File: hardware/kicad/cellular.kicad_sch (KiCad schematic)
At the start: 46 parts, among them J4 SMN-304, J5 BWIPX-1-001E, Q1 S8050, Q2 S8050, Q5 S8050, Q6 S8050, U2 A7670C_24x24mm

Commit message: wip: revision 2
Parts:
- removed C31, C32: TBD, Capacitor_SMD:C_0402_1005Metric, symbol Device:C_Small
- removed D7: PESD0402, Capacitor_SMD:C_0402_1005Metric, symbol Device:D_TVS
- removed J5: BWIPX-1-001E, SAMTEC_RSP-122811-02:SAMTEC_RSP-122811-02, symbol RSP-122811-02:RSP-122811-02
- removed JP1: A7670_BOOT, Jumper:SolderJumper-2_P1.3mm_Open_RoundedPad1.0x1.5mm, symbol Jumper:SolderJumper_2_Open
- removed R13: 10k, Resistor_SMD:R_0402_1005Metric, symbol Device:R_Small
- removed R20, R21: 0, Resistor_SMD:R_0402_1005Metric, symbol Device:R_Small
- added C29: 33p, Capacitor_SMD:C_0402_1005Metric, symbol Device:C_Small
- added TP11: USB_BOOT, TestPoint:TestPoint_Pad_D1.0mm, symbol Connector:TestPoint
- added TP12: UART_LOG_TXD, TestPoint:TestPoint_Pad_D1.0mm, symbol Connector:TestPoint
- Q1, Q2: value S8050 -> PMBT3904
- TP1: value VBUS -> USB_DP; footprint TestPoint:TestPoint_Pad_D1.5mm -> TestPoint:TestPoint_Pad_D1.0mm; Distributor - -> (none); Distributor Link - -> (none); Distributor Part Number - -> (none); Id 47 -> (none); Manufacture - -> (none); Manufacture Part Number - -> (none); Type SMD -> (none)
- TP2: value USB_DP -> USB_DM; footprint TestPoint:TestPoint_Pad_D1.5mm -> TestPoint:TestPoint_Pad_D1.0mm; Distributor - -> (none); Distributor Link - -> (none); Distributor Part Number - -> (none); Id 48 -> (none); Manufacture - -> (none); Manufacture Part Number - -> (none); Type SMD -> (none)
- TP3: value USB_DM -> VBUS; footprint TestPoint:TestPoint_Pad_D1.5mm -> TestPoint:TestPoint_Pad_D1.0mm; Distributor - -> (none); Distributor Link - -> (none); Distributor Part Number - -> (none); Id 49 -> (none); Manufacture - -> (none); Manufacture Part Number - -> (none); Type SMD -> (none)
- TP4: value GND -> UART_LOG_RXD; footprint TestPoint:TestPoint_Pad_D1.5mm -> TestPoint:TestPoint_Pad_D1.0mm; Distributor - -> (none); Distributor Link - -> (none); Distributor Part Number - -> (none); Id 50 -> (none); Manufacture - -> (none); Manufacture Part Number - -> (none); Type SMD -> (none)
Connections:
- net GND: now also C29.2; no longer TP4.1
- net USIM_VDD: now also C29.1
- net CELL_ANT: now reaches U2.60 (RF_ANT)
- net UART_LOG_RXD: now reaches U2.22 (UART_LOG_RX)
- net UART_LOG_RXD: now also TP4.1
- net UART_LOG_TXD: now reaches U2.23 (UART_LOG_TX)
- net UART_LOG_TXD: now also TP12.1
- net USB_DP: now reaches TP1.1
- net USB_DP: now also U2.27 (USB_DP); no longer U2.24 (VBUS)
- net USB_DM: now reaches TP2.1
- net USB_DM: now also U2.28 (USB_DM); no longer U2.27 (USB_DP)
- net VBUS: now reaches TP3.1
- net VBUS: now also U2.24 (VBUS); no longer U2.28 (USB_DM)
- net +3.3V renamed +3V3
- net A7670_BOOT renamed USB_BOOT
- net USB_BOOT: now also TP11.1
- net A7670_PWR renamed CELL_PWRKEY
- net A7670_RST renamed CELL_RESET
- net A7670_RX renamed CELL_RXD
- net A7670_STATUS renamed CELL_STATUS
- net A7670_TX renamed CELL_TXD
- net A7670_UART_RX renamed RXD
- net A7670_UART_TX renamed TXD
- net VBAT_CELL renamed CELL_BATT
- no-connect marks 38 -> 36
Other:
- note added: "Power Key"
- note added: "Pull to +1V8 for download mode"
- note added: "Sheets Connection"
- note added: "UART Debug Port"
- note added: "USB Debugging Port"
- note removed: "Antenna"
- note removed: "Boot"
- note removed: "Power"
- note removed: "Test Point For USB"
- moved on the sheet: C16, C17, C18, C19, C20, C21, C29, C35, C36, C37, D1, D4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

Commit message: wip: revision 2
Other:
- note added: "Cellular Module"
- note removed: "A7670C"
- moved on the sheet: D4, Q1, Q2, R10, R11, R12, R9

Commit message: Added Ignion Antenna
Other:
- moved on the sheet: C29

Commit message: update to KiCAD 8 and add cell power regulator
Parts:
- FB1: footprint Capacitor_SMD:C_0805_2012Metric -> Inductor_SMD:L_0805_2012Metric
- renumbered C29 to C25, C16 to C27, C17 to C28, C18 to C29, C19 to C30, C20 to C31, C21 to C32, C36 to C33, C37 to C34, C35 to C37, C36 to C38, C29 to C47, D5 to D4, D1 to D5, D4 to D7, Q6 to Q3, Q5 to Q4, Q1 to Q5, Q2 to Q6, R15 to R16, R14 to R17, R16 to R20, R26 to R22, R27 to R23, R25 to R26, R24 to R27, R9 to R29, R10 to R30, R11 to R31, R12 to R32, U2 to U9

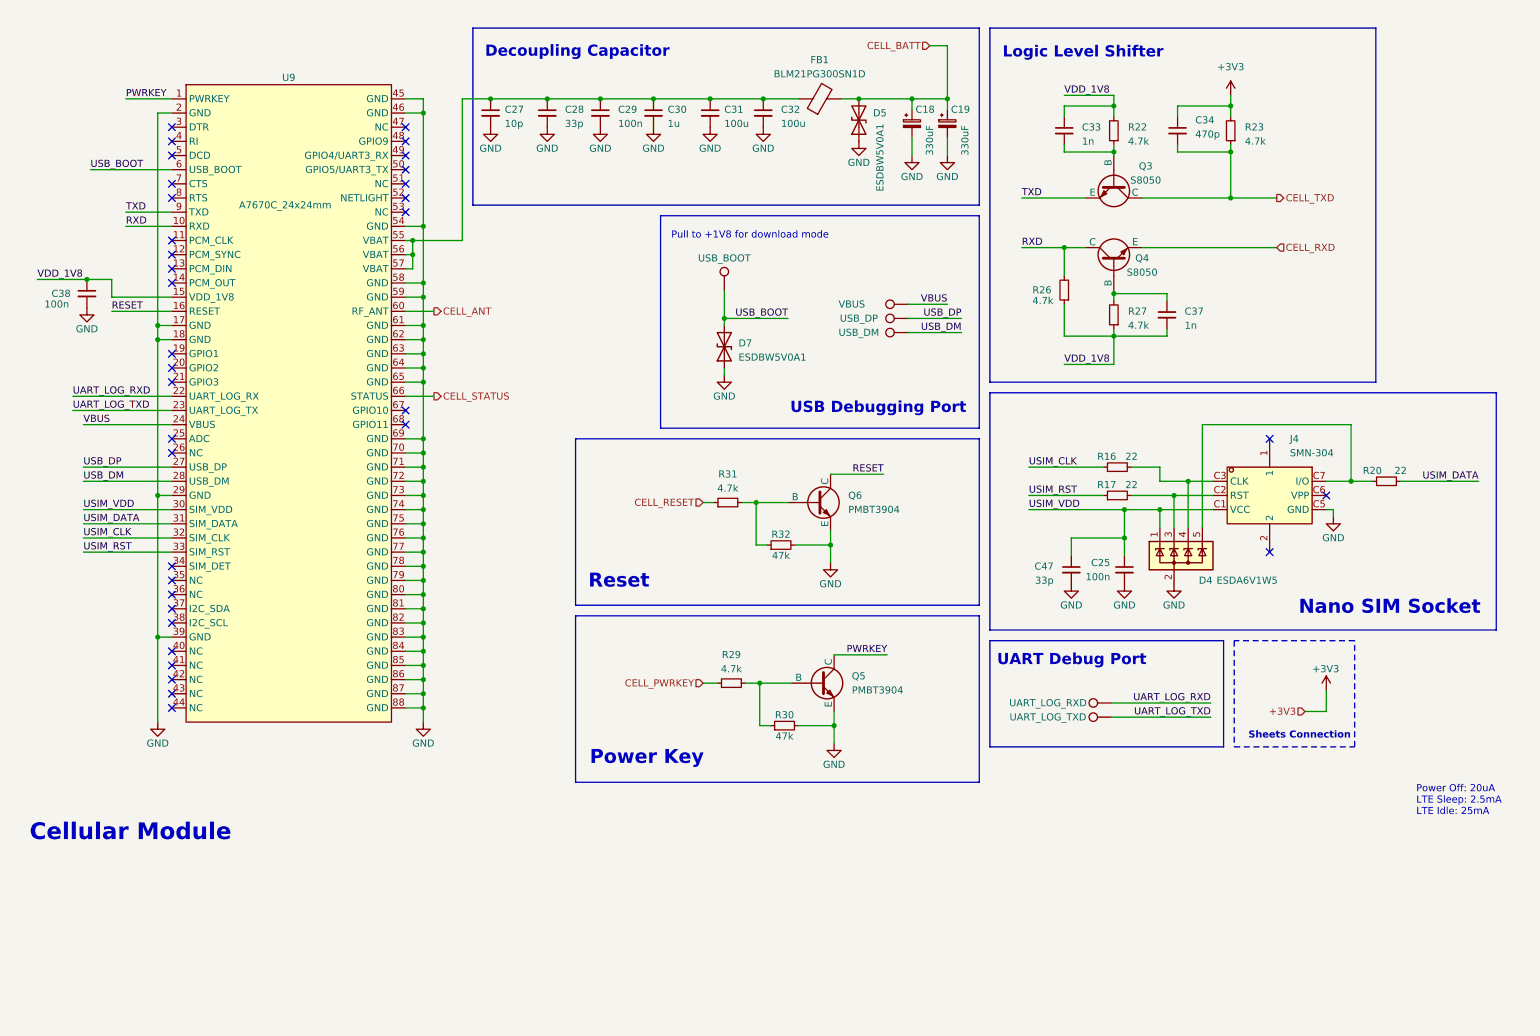
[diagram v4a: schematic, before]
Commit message: move components to use bwlc1a library
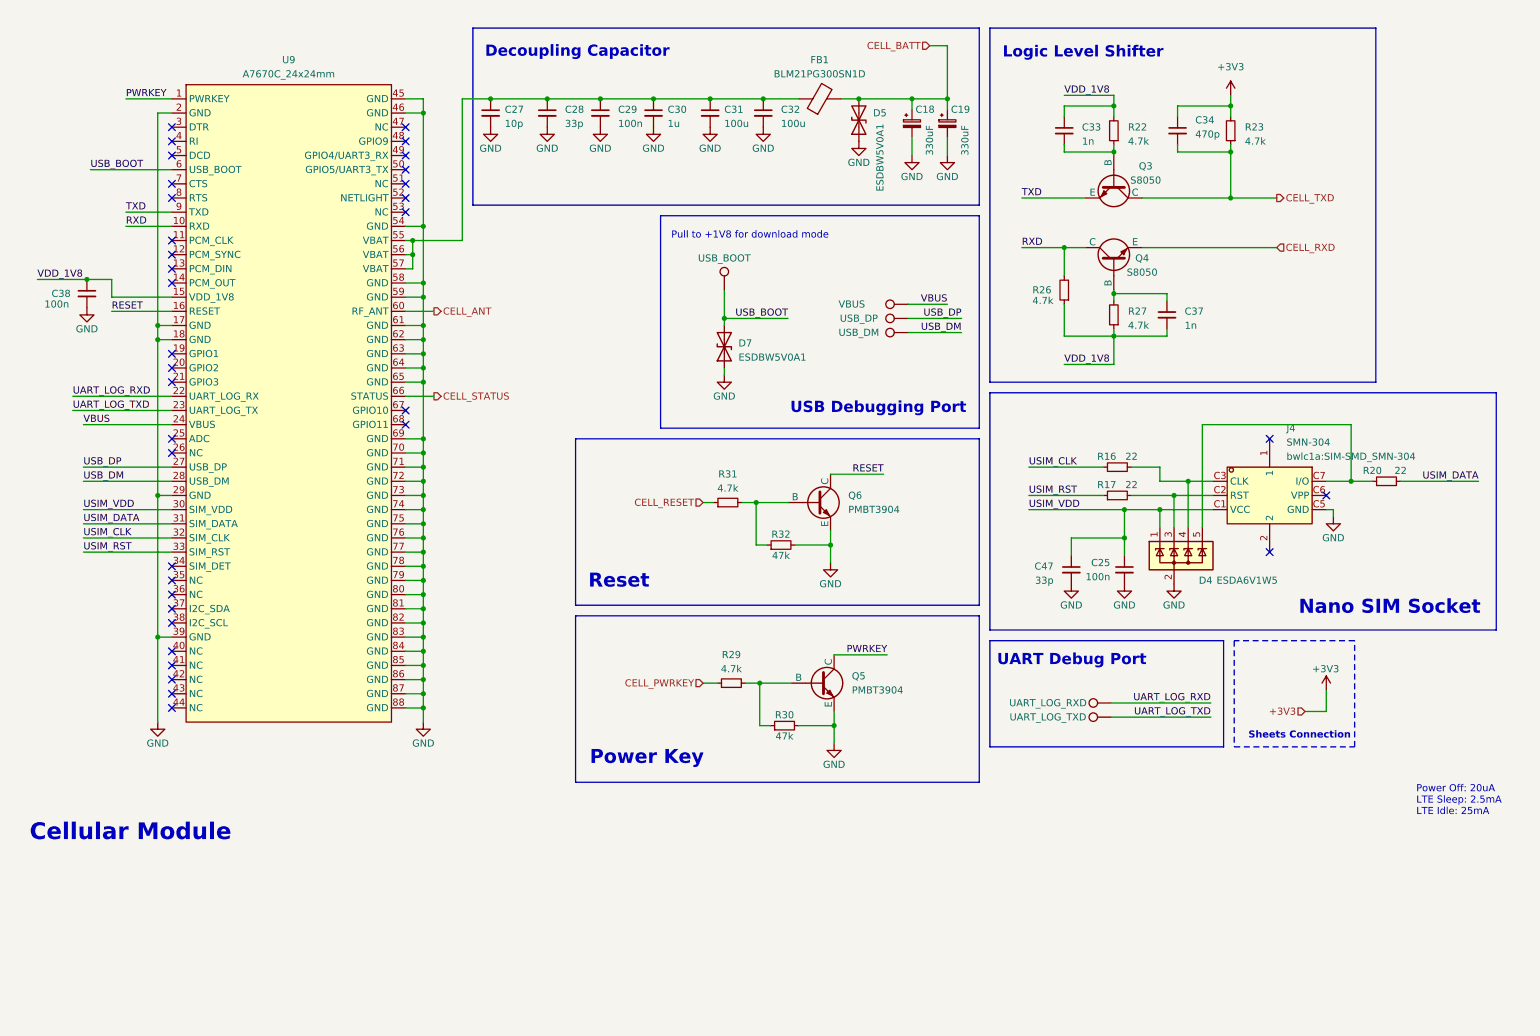
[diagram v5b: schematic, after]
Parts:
- J4: footprint SIM-SMD_SMN-304:SIM-SMD_SMN-304 -> bwlc1a:SIM-SMD_SMN-304; symbol SIM-SMD_SMN-304:SMN-304 -> bwlc1a:SMN-304
- U9: footprint A7670C:LGA-124_L24.0-W24.0-P1.0-A7670C-LASS -> bwlc1a:LGA-124_L24.0-W24.0-P1.0-A7670C-LASS; symbol Teapot:A7670X -> bwlc1a:A7670X
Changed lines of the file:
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@@
 	)
 	(symbol
-		(lib_id "SIM-SMD_SMN-304:SMN-304")
+		(lib_id "bwlc1a:SMN-304")
 		(at 239.395 100.965 270)
 		(unit 1)
@@
 		(fields_autoplaced yes)
 		(property "Reference" "J4"
-			(at 243.0211 90.805 90)
+			(at 242.4115 88.9 90)
 			(effects
 				(font
@@
 		)
 		(property "Value" "SMN-304"
-			(at 243.0211 93.345 90)
+			(at 242.4115 91.44 90)
 			(effects
 				(font
@@
 			)
 		)
-		(property "Footprint" "SIM-SMD_SMN-304:SIM-SMD_SMN-304"
-			(at 221.615 100.965 0)
-			(effects
-				(font
-					(size 1.27 1.27)
-				)
-				(hide yes)
-			)
-		)
-		(property "Datasheet" "~"
+		(property "Footprint" "bwlc1a:SIM-SMD_SMN-304"
+			(at 242.4115 93.98 90)
+			(effects
+				(font
+					(size 1.27 1.27)
+				)
+				(justify left)
+			)
+		)
+		(property "Datasheet" "https://lcsc.com/product-detail/Connector-Card-Sockets_XUNPU-SMN-304_C266889.html"
 			(at 219.075 100.965 0)
 			(effects
@@
 		)
 		(property "Type" "SMD"
+			(at 239.395 100.965 0)
+			(effects
+				(font
+					(size 1.27 1.27)
+				)
+				(hide yes)
+			)
+		)
+		(property "Manufacturer" ""
+			(at 239.395 100.965 0)
+			(effects
+				(font
+					(size 1.27 1.27)
+				)
+				(hide yes)
+			)
+		)
+		(property "Manufacturer Part Number" ""
 			(at 239.395 100.965 0)
 			(effects
@@
 	)
 	(symbol
-		(lib_id "Teapot:A7670X")
+		(lib_id "bwlc1a:A7670X")
 		(at 64.135 83.185 0)
 		(unit 1)
@@
 		(fields_autoplaced yes)
 		(property "Reference" "U9"
-			(at 63.5 26.035 0)
+			(at 63.5 22.86 0)
 			(effects
 				(font
@@
 		)
 		(property "Value" "A7670C_24x24mm"
-			(at 62.865 48.895 0)
-			(effects
-				(font
-					(size 1.27 1.27)
-				)
-			)
-		)
-		(property "Footprint" "A7670C:LGA-124_L24.0-W24.0-P1.0-A7670C-LASS"
-			(at 62.865 48.895 0)
+			(at 63.5 25.4 0)
+			(effects
+				(font
+					(size 1.27 1.27)
+				)
+			)
+		)
+		(property "Footprint" "bwlc1a:LGA-124_L24.0-W24.0-P1.0-A7670C-LASS"
+			(at 64.135 26.035 0)
 			(effects
 				(font
@@
 			(at 64.135 83.185 0)
 			(effects
+				(font
+					(size 1.27 1.27)
+				)
+				(hide yes)
+			)
+		)
+		(property "Manufacturer" ""
+			(at 64.135 83.185 0)
+			(effects
+				(font
+					(size 1.27 1.27)
+				)
+				(hide yes)
+			)
+		)
+		(property "Manufacturer Part Number" ""
+			(at 64.135 83.185 0)
+			(effects

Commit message: update bill of materials
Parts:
- C18, C19: value 330uF -> 330u; footprint Capacitor_Tantalum_SMD:CP_EIA-3528-15_AVX-H_Pad1.50x2.35mm_HandSolder -> Capacitor_Tantalum_SMD:CP_EIA-3528-21_Kemet-B; Distributor (none) -> LCSC; Distributor Link (none) -> https://www.lcsc.com/product-detail/Tantalum-Capacitors_KEM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; Distributor Part Number (none) -> C696806; Manufacturer (none) -> KEMET; Manufacturer Part Number (none) -> T520B337M006ATE040
- C25, C29, C38: Id 3 -> (none); Manufacture Samsung Electro-Mechanics -> (none); Manufacture Part Number CL05B104KO5NNNC -> (none); Manufacturer (none) -> Samsung Electro-Mechanics; Manufacturer Part Number (none) -> CL05B104KO5NNNC; Type SMD -> (none)
- C27: Id 10 -> (none); Manufacture YAGEO -> (none); Manufacture Part Number CC0402JRNPO9BN100 -> (none); Manufacturer (none) -> YAGEO; Manufacturer Part Number (none) -> CC0402JRNPO9BN100; Type SMD -> (none)
- C28: Id 11 -> (none); Manufacture FH (Guangdong Fenghua Advanced Tech) -> (none); Manufacture Part Number 0402CG330J500NT -> (none); Manufacturer (none) -> FH (Guangdong Fenghua Advanced Tech); Manufacturer Part Number (none) -> 0402CG330J500NT; Type SMD -> (none)
- C30: Id 12 -> (none); Manufacture Samsung Electro-Mechanics -> (none); Manufacture Part Number CL05A105KP5NNNC -> (none); Manufacturer (none) -> Samsung Electro-Mechanics; Manufacturer Part Number (none) -> CL05A105KP5NNNC; Type SMD -> (none)
- C31, C32: Id 13 -> (none); Manufacture Murata Electronics -> (none); Manufacture Part Number GRM21BR60J107ME15L -> (none); Manufacturer (none) -> Murata Electronics; Manufacturer Part Number (none) -> GRM21BR60J107ME15L; Type SMD -> (none)
- C33, C37: Id 14 -> (none); Manufacture Samsung Electro-Mechanics -> (none); Manufacture Part Number CL05B102KB5NNNC -> (none); Manufacturer (none) -> Samsung Electro-Mechanics; Manufacturer Part Number (none) -> CL05B102KB5NNNC; Type SMD -> (none)
- C34: Id 15 -> (none); Manufacture YAGEO -> (none); Manufacturer (none) -> YAGEO; Manufacturer Part Number (none) -> CC0402KRX7R9BB471; Type SMD -> (none)
- C47: Distributor Link https://www.lcsc.com/product-detail/Multilayer-Ceramic-Capacitors-MLCC-SMD-SMT_Samsung-Electro-Mechanics-CL05B104KO5NNNC_C1525.html -> https://www.lcsc.com/product-detail/Multilayer-Ceramic-Capacitors-MLCC-SMD-SMT_FH-Guangdong-Fenghua-Advanced-Tech-0402CG330J500NT_C1562.html; Distributor Part Number C1525 -> C1562; Id 3 -> (none); Manufacture Samsung Electro-Mechanics -> (none); Manufacture Part Number CL05B104KO5NNNC -> (none); Manufacturer (none) -> FH (Guangdong Fenghua Advanced Tech); Manufacturer Part Number (none) -> 0402CG330J500NT; Type SMD -> (none)
- D4: Id 20 -> (none); Manufacture TECH PUBLIC -> (none); Manufacture Part Number ESDA6V1W5-TP -> (none); Manufacturer (none) -> TECH PUBLIC; Manufacturer Part Number (none) -> ESDA6V1W5-TP; Type SMD -> (none)
- D5, D7: footprint Capacitor_SMD:C_0402_1005Metric -> Diode_SMD:D_SOD-882; Id 19 -> (none); Manufacture Leiditech -> (none); Manufacture Part Number ESDBW5V0A1 -> (none); Manufacturer (none) -> Leiditech; Manufacturer Part Number (none) -> ESDBW5V0A1; Type SMD -> (none)
- FB1: Id 23 -> (none); Manufacture Murata Electronics -> (none); Manufacture Part Number BLM21PG300SN1D -> (none); Manufacturer (none) -> Murata Electronics; Manufacturer Part Number (none) -> BLM21PG300SN1D; Type SMD -> (none)
- J4: Id 27 -> (none); Manufacture Part Number SMN-304 -> (none); Manufacturer (none) -> XUNPU; Manufacturer Part Number (none) -> SMN-304; Type SMD -> (none)
- Q3, Q4, Q5, Q6: Id 34 -> (none); Manufacture Guangdong Hottech -> (none); Manufacture Part Number S8050 -> (none); Manufacturer (none) -> Guangdong Hottech; Manufacturer Part Number (none) -> S8050; Type SMD -> (none)
- R16, R17, R20: Id 43 -> (none); Manufacture UNI-ROYAL(Uniroyal Elec) -> (none); Manufacture Part Number 0402WGF220JTCE -> (none); Manufacturer (none) -> UNI-ROYAL(Uniroyal Elec); Manufacturer Part Number (none) -> 0402WGF220JTCE; Type SMD -> (none)
- R22, R23, R26, R27, R29, R31: value 4.7k -> 4k7; Id 39 -> (none); Manufacture UNI-ROYAL(Uniroyal Elec) -> (none); Manufacture Part Number 0402WGJ0472TCE -> (none); Manufacturer (none) -> UNI-ROYAL(Uniroyal Elec); Manufacturer Part Number (none) -> 0402WGJ0472TCE; Type SMD -> (none)
- R30, R32: Id 41 -> (none); Manufacture UNI-ROYAL(Uniroyal Elec) -> (none); Manufacture Part Number 0402WGF4702TCE -> (none); Manufacturer (none) -> UNI-ROYAL(Uniroyal Elec); Manufacturer Part Number (none) -> 0402WGF4702TCE; Type SMD -> (none)
- U9: value A7670C_24x24mm -> A7670C; Distributor Link https://www.lcsc.com/product-detail/2G-3G-4G-5G-Modules_SIMCom-Wireless-Solutions-A7670C-LASE_C2888406.html -> https://www.lcsc.com/product-detail/2G-3G-4G-5G-Modules_SIMCom-Wireless-Solutions-A7670C-MASL_C2891912.html; Distributor Part Number C2888406 -> C2891912; Id 59 -> (none); Manufacture SIMCom Wireless Solutions -> (none); Manufacture Part Number A7670C-LASE -> (none); Manufacturer (none) -> SIMCom Wireless Solutions; Manufacturer Part Number (none) -> A7670C-MASL; Type SMD -> (none)
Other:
- note added: "* common antenna range : 824MHz~960MHz 1710MHz~2170MHz 1710MHz~2690MHz"
- note added: "* most US operator uses band 5"
- note added: "2G DL UL ----------------------------- EGSM900 925~960 MHz 880~915 MHz DCS1800 1805~1880 MHz 1710~1785 MHz LTE Band UL Freq. DL Freq. DuplexMode ---------------------------------------- 1 1920~1980 MHz 2110~2170 MHz FDD 3 1710~1785 MHz 1805~1880 MHz FDD 5 869~894 MHz 824~849 MHz FDD 8 880~915 MHz 925~960 MHz FDD 34 2010~2025 MHz 2010~2025 MHz TDD 38 2570~2620 MHz 2570~2620 MHz TDD 39 1880~1920 MH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"
- note added: "A7670C Frequency"
- note added: "Power Profile"
- moved on the sheet: C18, C19, C27, C28, C29, C30, C31, C32, C38, D5, FB1, U9

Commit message: add page info
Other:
- company: (none) -> Teapot Laboratories
- title: (none) -> Cellular
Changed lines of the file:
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@@
 	(generator_version "8.0")
 	(paper "A4")
+	(title_block
+		(title "Cellular")
+		(date "2024-05-17")
+		(rev "1")
+		(company "Teapot Laboratories")
+	)
 	(junction
 		(at 85.725 121.92)
